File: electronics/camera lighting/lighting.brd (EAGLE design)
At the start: 26 x 26 mm, 10 parts

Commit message: pre-production PCBs
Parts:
- renumbered P1 to PWR
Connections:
- net 5V: now also PWR.2; no longer PWR.1
- net GND: now also PWR.1; no longer PWR.2
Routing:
- net 5V: track 8.04 -> 10.7 mm
- net GND: track 11.7 -> 13.7 mm
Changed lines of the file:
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@@
 <attribute name="VALUE" x="14.27" y="5.54" size="1.27" layer="27" rot="R180"/>
 </element>
-<element name="P1" library="jst-ph" package="JST-PH2" value="" x="17.75" y="1.75" smashed="yes" rot="MR0"/>
+<element name="PWR" library="jst-ph" package="JST-PH2" value="" x="17.75" y="1.75" smashed="yes" rot="MR0"/>
 </elements>
 <signals>
 <signal name="5V">
 <contactref element="R1" pad="2"/>
-<contactref element="P1" pad="1"/>
-<wire x1="8.922" y1="1.25" x2="16.25" y2="1.25" width="0.25" layer="1"/>
-<wire x1="16.25" y1="1.25" x2="16.75" y2="1.75" width="0.25" layer="1"/>
+<contactref element="PWR" pad="2"/>
+<wire x1="18.75" y1="1.75" x2="17.5" y2="0.5" width="0.25" layer="1"/>
+<wire x1="17.5" y1="0.5" x2="9.672" y2="0.5" width="0.25" layer="1"/>
+<wire x1="9.672" y1="0.5" x2="8.922" y2="1.25" width="0.25" layer="1"/>
 </signal>
 <signal name="GND">
@@
 <vertex x="0" y="26"/>
 </polygon>
-<contactref element="P1" pad="2"/>
 <via x="2.75" y="7.25" extent="1-16" drill="0.3"/>
 <via x="3" y="16" extent="1-16" drill="0.3"/>
@@
 <wire x1="23.249996875" y1="18.75" x2="23.25" y2="18.75" width="0.25" layer="1"/>
 <wire x1="23" y1="11.25" x2="23" y2="10" width="0.25" layer="1"/>
-<wire x1="19.7625625" y1="3.7625625" x2="18.75" y2="2.75" width="0.25" layer="1"/>
-<wire x1="18.75" y1="2.75" x2="18.75" y2="1.75" width="0.25" layer="1"/>
 <via x="10" y="3" extent="1-16" drill="0.3"/>
 <wire x1="11.25" y1="3" x2="10" y2="3" width="0.25" layer="1"/>
+<contactref element="PWR" pad="1"/>
+<wire x1="19.7625625" y1="3.7625625" x2="17.7625625" y2="3.7625625" width="0.25" layer="1"/>
+<wire x1="17.7625625" y1="3.7625625" x2="16.75" y2="2.75" width="0.25" layer="1"/>
+<wire x1="16.75" y1="2.75" x2="16.75" y2="1.75" width="0.25" layer="1"/>
 </signal>
 <signal name="COMMON">

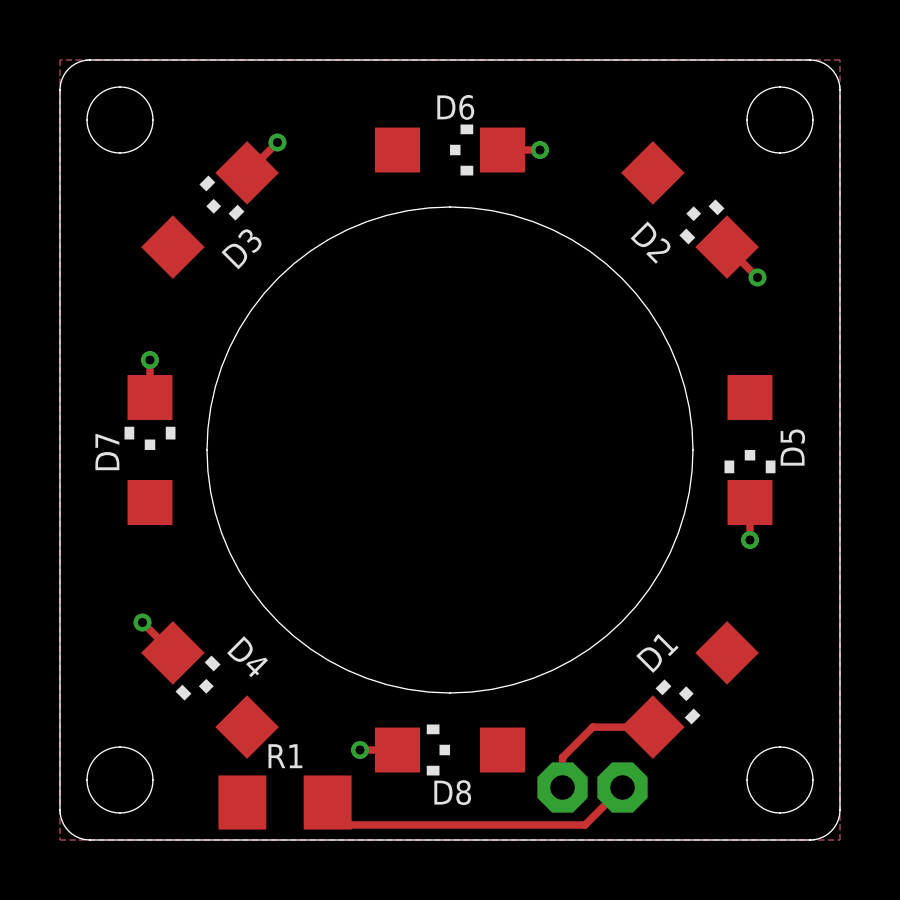
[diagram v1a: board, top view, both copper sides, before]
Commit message: updated all PCBs and added PDF schematics
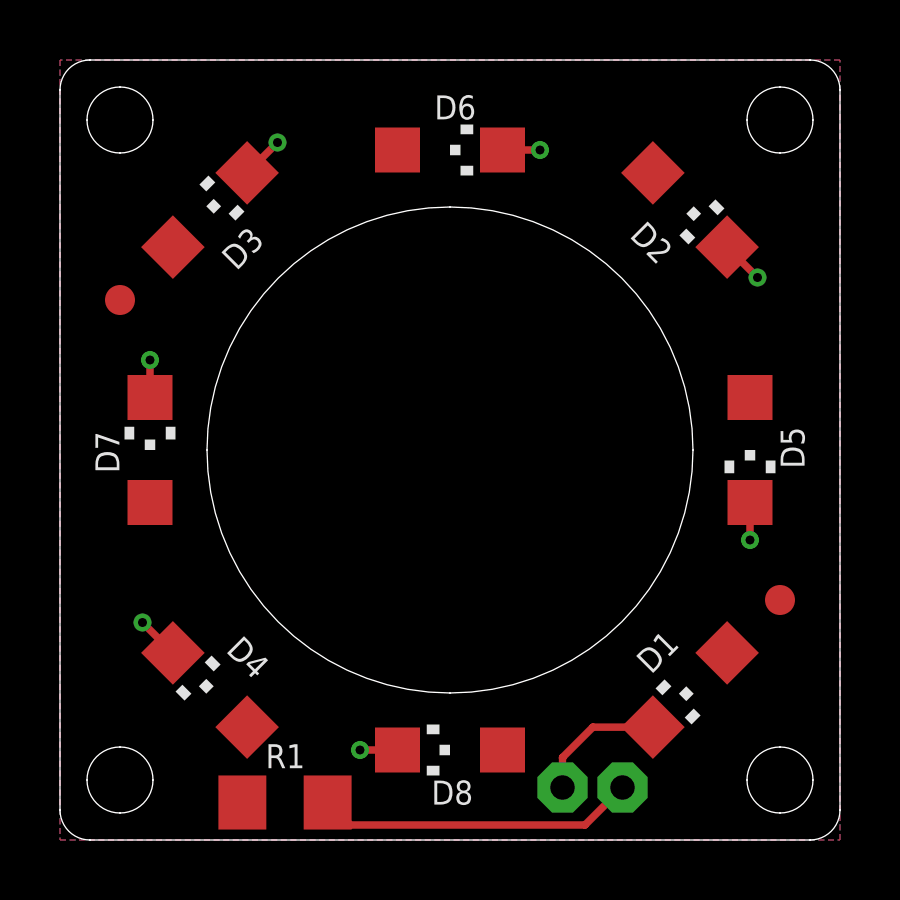
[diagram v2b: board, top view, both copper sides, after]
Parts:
- added U$1, U$2: FIDUCIAL, adafruit:FIDUCIAL_1MM
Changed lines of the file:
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@@
 <circle x="2" y="24" radius="2" width="0.1" layer="39"/>
 <circle x="2" y="2" radius="2" width="0.1" layer="39"/>
-<text x="14.5" y="2.75" size="1" layer="26" ratio="10" rot="MR270">5V</text>
-<text x="21" y="0.75" size="1" layer="26" ratio="10" rot="MR90">GND</text>
+<text x="14.5" y="2.75" size="1" layer="26" font="vector" ratio="10" rot="MR270">5V</text>
+<text x="21" y="0.75" size="1" layer="26" font="vector" ratio="10" rot="MR90">GND</text>
 </plain>
 <attributes>
@@
 <elements>
 <element name="D1" library="adafruit" package="CHIPLED_1206" value="" x="21" y="5" smashed="yes" rot="R135">
-<attribute name="NAME" x="19.70395" y="5.5" size="0.8" layer="25" rot="R45"/>
+<attribute name="NAME" x="19.70395" y="5.5" size="0.8" layer="25" font="vector" rot="R45"/>
 <attribute name="VALUE" x="20.101971875" y="7.694075" size="1.27" layer="27" rot="R225"/>
 </element>
 <element name="D2" library="adafruit" package="CHIPLED_1206" value="" x="21" y="21" smashed="yes" rot="R225">
-<attribute name="NAME" x="20.5" y="19.70395" size="0.8" layer="25" rot="R135"/>
+<attribute name="NAME" x="20.5" y="19.70395" size="0.8" layer="25" font="vector" rot="R135"/>
 <attribute name="VALUE" x="18.305921875" y="20.101971875" size="1.27" layer="27" rot="R315"/>
 </element>
 <element name="D3" library="adafruit" package="CHIPLED_1206" value="" x="5" y="21" smashed="yes" rot="R315">
-<attribute name="NAME" x="6.296053125" y="20.5" size="0.8" layer="25" rot="R225"/>
+<attribute name="NAME" x="6.296053125" y="20.5" size="0.8" layer="25" font="vector" rot="R225"/>
 <attribute name="VALUE" x="5.898025" y="18.305921875" size="1.27" layer="27" rot="R45"/>
 </element>
 <element name="D4" library="adafruit" package="CHIPLED_1206" value="" x="5" y="5" smashed="yes" rot="R45">
-<attribute name="NAME" x="5.5" y="6.296053125" size="0.8" layer="25" rot="R315"/>
+<attribute name="NAME" x="5.5" y="6.296053125" size="0.8" layer="25" font="vector" rot="R315"/>
 <attribute name="VALUE" x="7.694075" y="5.898025" size="1.27" layer="27" rot="R135"/>
 </element>
 <element name="R1" library="adafruit" package="R1206" value="330" x="7.5" y="1.25" smashed="yes">
-<attribute name="NAME" x="6.853" y="2.393" size="0.8" layer="25"/>
+<attribute name="NAME" x="6.853" y="2.393" size="0.8" layer="25" font="vector"/>
 <attribute name="VALUE" x="6.103" y="-1.163" size="1.27" layer="27"/>
 </element>
 <element name="D5" library="adafruit" package="CHIPLED_1206" value="" x="23" y="13" smashed="yes" rot="R180">
-<attribute name="NAME" x="24.02" y="13.77" size="0.8" layer="25" rot="R270"/>
+<attribute name="NAME" x="24.02" y="13.77" size="0.8" layer="25" font="vector" rot="R270"/>
 <attribute name="VALUE" x="20.46" y="14.27" size="1.27" layer="27" rot="R270"/>
 </element>
 <element name="D6" library="adafruit" package="CHIPLED_1206" value="" x="13" y="23" smashed="yes" rot="R270">
-<attribute name="NAME" x="12.48" y="24.02" size="0.8" layer="25"/>
+<attribute name="NAME" x="12.48" y="24.02" size="0.8" layer="25" font="vector"/>
 <attribute name="VALUE" x="11.73" y="20.46" size="1.27" layer="27"/>
 </element>
 <element name="D7" library="adafruit" package="CHIPLED_1206" value="" x="3" y="13" smashed="yes">
-<attribute name="NAME" x="1.98" y="12.23" size="0.8" layer="25" rot="R90"/>
+<attribute name="NAME" x="1.98" y="12.23" size="0.8" layer="25" font="vector" rot="R90"/>
 <attribute name="VALUE" x="5.54" y="11.73" size="1.27" layer="27" rot="R90"/>
 </element>
 <element name="D8" library="adafruit" package="CHIPLED_1206" value="" x="13" y="3" smashed="yes" rot="R90">
-<attribute name="NAME" x="13.77" y="1.98" size="0.8" layer="25" rot="R180"/>
+<attribute name="NAME" x="13.77" y="1.98" size="0.8" layer="25" font="vector" rot="R180"/>
 <attribute name="VALUE" x="14.27" y="5.54" size="1.27" layer="27" rot="R180"/>
 </element>
 <element name="PWR" library="jst-ph" package="JST-PH2" value="" x="17.75" y="1.75" smashed="yes" rot="MR0"/>
+<element name="U$1" library="adafruit" package="FIDUCIAL_1MM" value="FIDUCIAL" x="2" y="18"/>
+<element name="U$2" library="adafruit" package="FIDUCIAL_1MM" value="FIDUCIAL" x="24" y="8"/>
 </elements>
 <signals>
